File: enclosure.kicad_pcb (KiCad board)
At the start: 2 copper layers, 100 x 220 mm, 184 parts, among them J101 Conn_01x06_Socket, J102 Conn_01x02_Socket, J103 Conn_01x02_Socket, J104 Conn_01x02_Socket, J105 Conn_01x02_Socket, Q1001 DPLS350E, U1001 MC7805, U1002 MC7812, U101 4041, U201 Si8641BD-B-IS2, U202 R05C05TE05S, U301 SN74LVC1G04DBVR, U302 AD567xR, U401 LTC6992IS6-1, U501 LTC6992IS6-1, U601 LTC6992IS6-1, U701 VNH7070ASTR, U801 VNH7070ASTR, U901 VNH7070ASTR

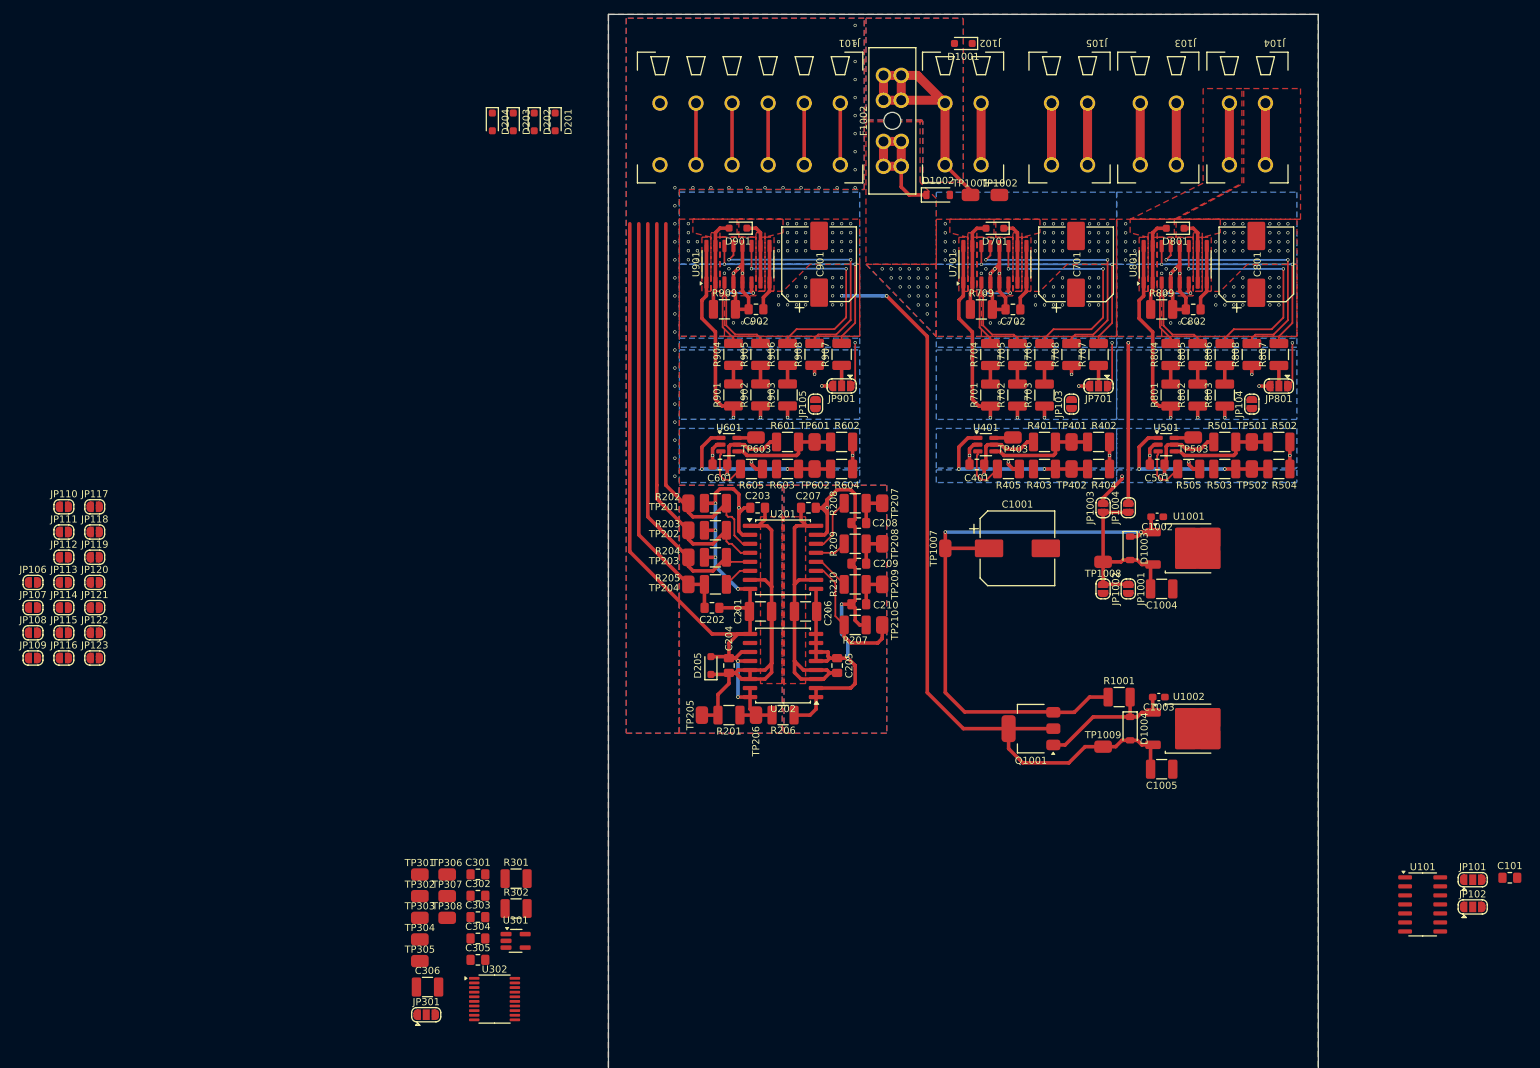
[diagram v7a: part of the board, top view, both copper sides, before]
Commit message: add dac sub-layout
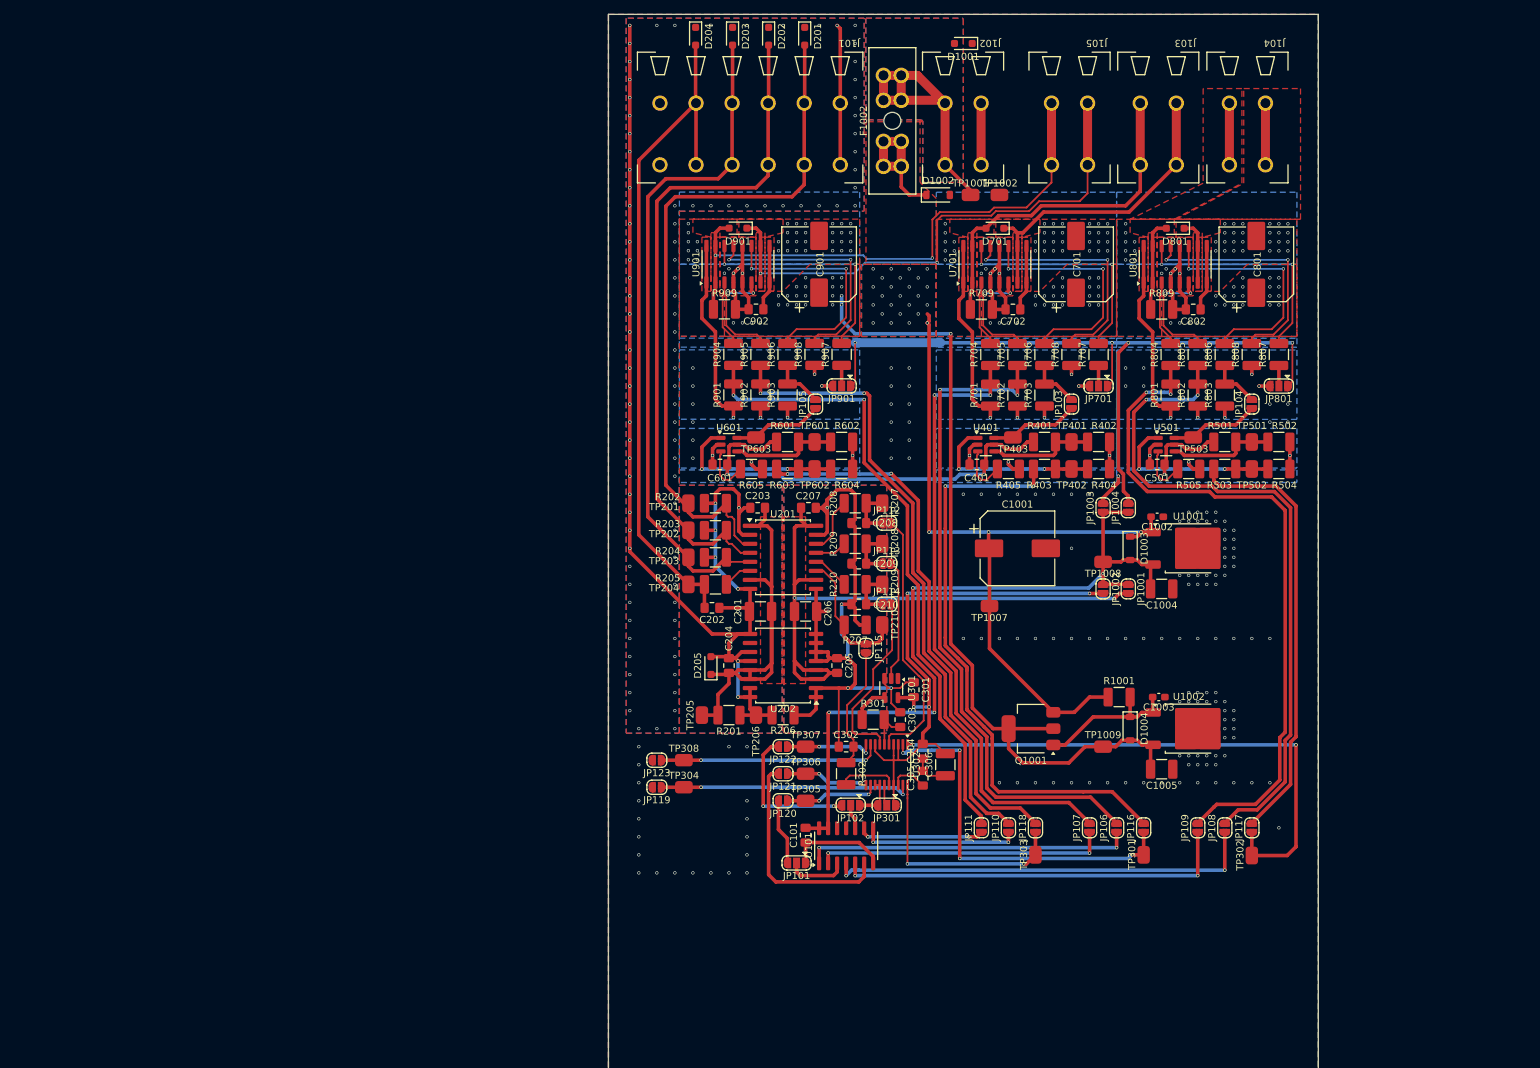
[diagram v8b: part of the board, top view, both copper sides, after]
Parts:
- moved JP108 170.1 mm to (236.8, 154.6), turned to 90 degrees
- moved JP117 169.2 mm to (240.6, 154.6), turned to 90 degrees
- moved JP109 165.8 mm to (233.0, 154.6), turned to 90 degrees
- moved JP106 156.5 mm to (221.6, 154.6), turned to 90 degrees
- moved JP116 154.0 mm to (225.4, 154.6), turned to 90 degrees
- moved JP107 152.0 mm to (217.8, 154.6), turned to 90 degrees
- moved JP110 140.5 mm to (206.3, 154.6), turned to 90 degrees
- moved JP118 138.9 mm to (210.2, 154.6), turned to 90 degrees
- moved JP111 135.8 mm to (202.5, 154.6), turned to 90 degrees
- moved TP302 117.3 mm to (240.6, 158.5), turned to 90 degrees
- moved JP112 116.0 mm to (189.2, 111.7)
- moved JP113 115.9 mm to (189.2, 117.4)
- moved JP114 115.9 mm to (189.2, 123.1)
- moved JP115 113.0 mm to (186.3, 129.3), turned to -90 degrees
- moved TP301 102.0 mm to (225.4, 158.4), turned to 90 degrees
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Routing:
- net /full-bridge1/IN_A: track 2.61 -> 96.6 mm, vias 0 -> 2
- net /full-bridge1/IN_B: track 2.61 -> 96.5 mm, vias 0 -> 2
- net /full-bridge/IN_B: track 2.61 -> 94.6 mm, vias 0 -> 2
- net /full-bridge2/IN_A: track 2.61 -> 89.4 mm, vias 0 -> 2
- net /full-bridge2/IN_B: track 2.61 -> 88.7 mm, vias 0 -> 2
- net /full-bridge/IN_A: track 2.61 -> 87.7 mm, vias 0 -> 2
- net /dac_ch_0: track 0.00 -> 83.3 mm, vias 0 -> 2
- net +5VA: track 27.7 -> 108.5 mm, vias 0 -> 4
- net +5VA_dac: track 0.00 -> 80.1 mm, vias 0 -> 4
- net /dac/dac_ch_1: track 0.00 -> 79.1 mm, vias 0 -> 2
- net /dac_ch_2: track 0.00 -> 76.6 mm, vias 0 -> 2
- net +5VA_full-bridge: track 41.6 -> 104.4 mm
- net /dac_ch_1: track 0.00 -> 62.0 mm
- net Net-(JP108-A): track 0.00 -> 60.7 mm, vias 0 -> 2
- net /fan_-: track 17.9 -> 76.2 mm, vias 0 -> 2
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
